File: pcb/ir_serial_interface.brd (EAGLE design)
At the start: 41.6 x 24.2 mm, 27 parts, among them IC1 PIC18LF2550, IC2 LP2992, Q2 MMBT6428LT1G, T1 PS401

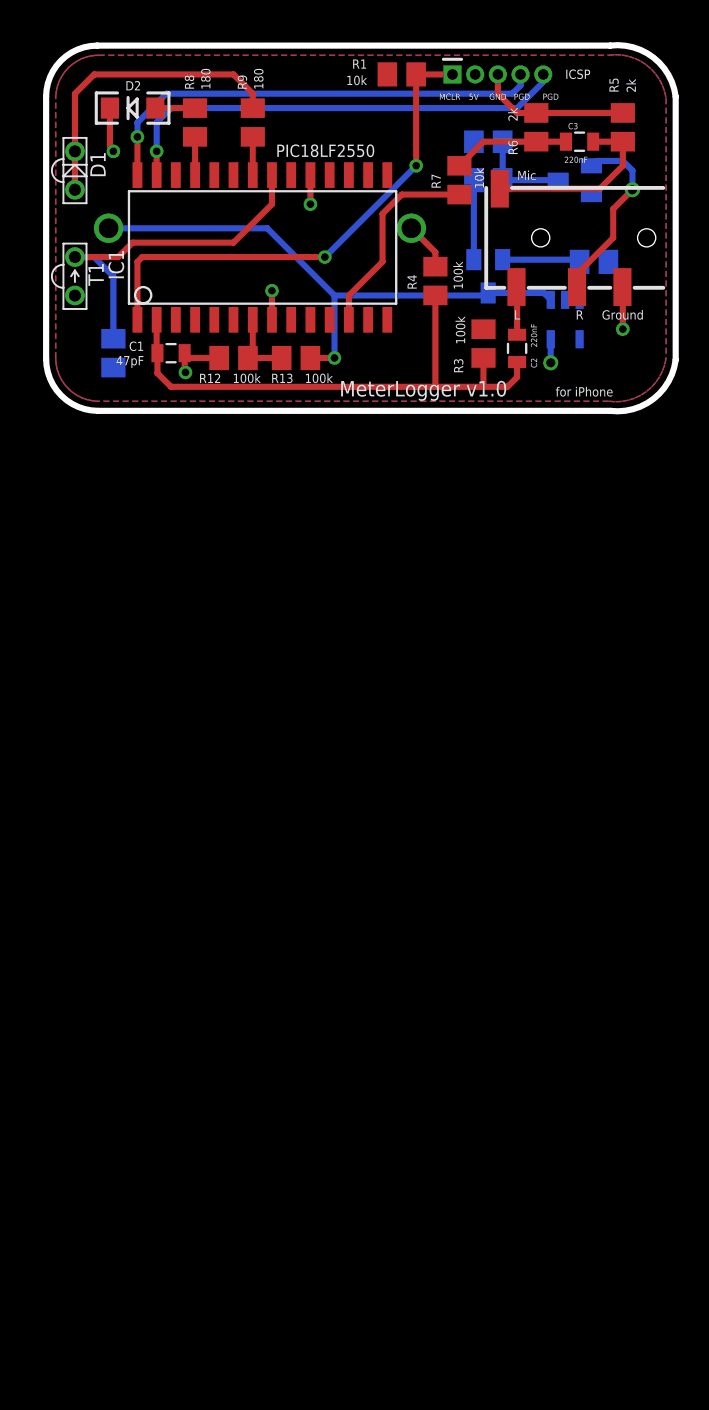
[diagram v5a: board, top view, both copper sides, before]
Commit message: PCB: Martens rettelser
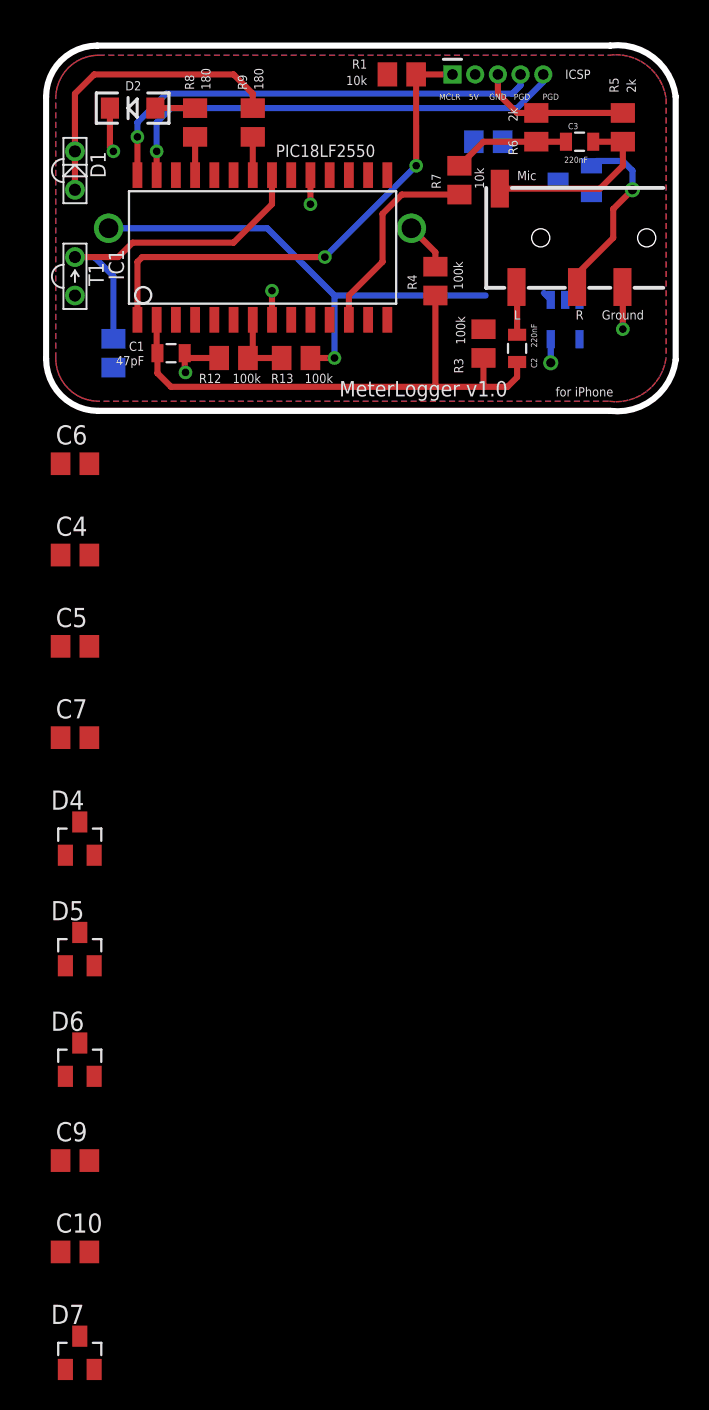
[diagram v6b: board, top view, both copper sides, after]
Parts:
- removed Q2: MMBT6428LT1G, transistor-npn:SOT23
- removed R10: 2k, resistor:M0805
- removed R11: 100k, resistor:M0805
- added C10, C7, C8, C9: 220nF, rcl:C0805
- added C5: 10uF, rcl:C0805
- added C6: 2200nF, rcl:C0805
- added D4, D5, D6: BAT65-05, diode:SOT23
- added D7: (no value), diode:SOT23
- C4: value 220nF -> 10nF
- moved C4 38.6 mm to (24.1, 16.5), flipped to the top
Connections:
- new net N$21: C10.2, D6.3, D7.3, IC2.3
- new net N$22: C4.1, IC2.4
- net +5V: now also C5.1
- net GND: now also C5.2, C6.2, C8.1, D3.1, D7.1; no longer R11.2
- net N$12: now also C7.1; no longer D3.1
- net N$13: now also C7.2, C9.1, D3.3, D4.1; no longer IC2.3, Q2.2, R11.1
- net N$17: now also C9.2, D5.3, D6.1; no longer Q2.1, R10.1
- net N$18: now also C10.1, C8.2, D4.3, D5.1; no longer C4.1, D3.3, R10.2
- net V+: now also C6.1; no longer Q2.3
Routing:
- net N$13: track 7.65 -> 0.00 mm
- net N$18: track 6.20 -> 0.00 mm
- net N$17: track 5.25 -> 0.00 mm
- net V+: track 37.0 -> 33.1 mm

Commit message: PCB: missing zener
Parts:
- D7: value (none) -> MMBZ5231BLT1G
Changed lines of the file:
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@@
 <element name="C9" library="rcl" package="C0805" value="220nF" x="24.13" y="-23.495"/>
 <element name="C10" library="rcl" package="C0805" value="220nF" x="24.13" y="-29.5275"/>
-<element name="D7" library="diode" package="SOT23" value="" x="24.4475" y="-36.195"/>
+<element name="D7" library="diode" package="SOT23" value="MMBZ5231BLT1G" x="24.4475" y="-36.195"/>
 </elements>
 <signals>

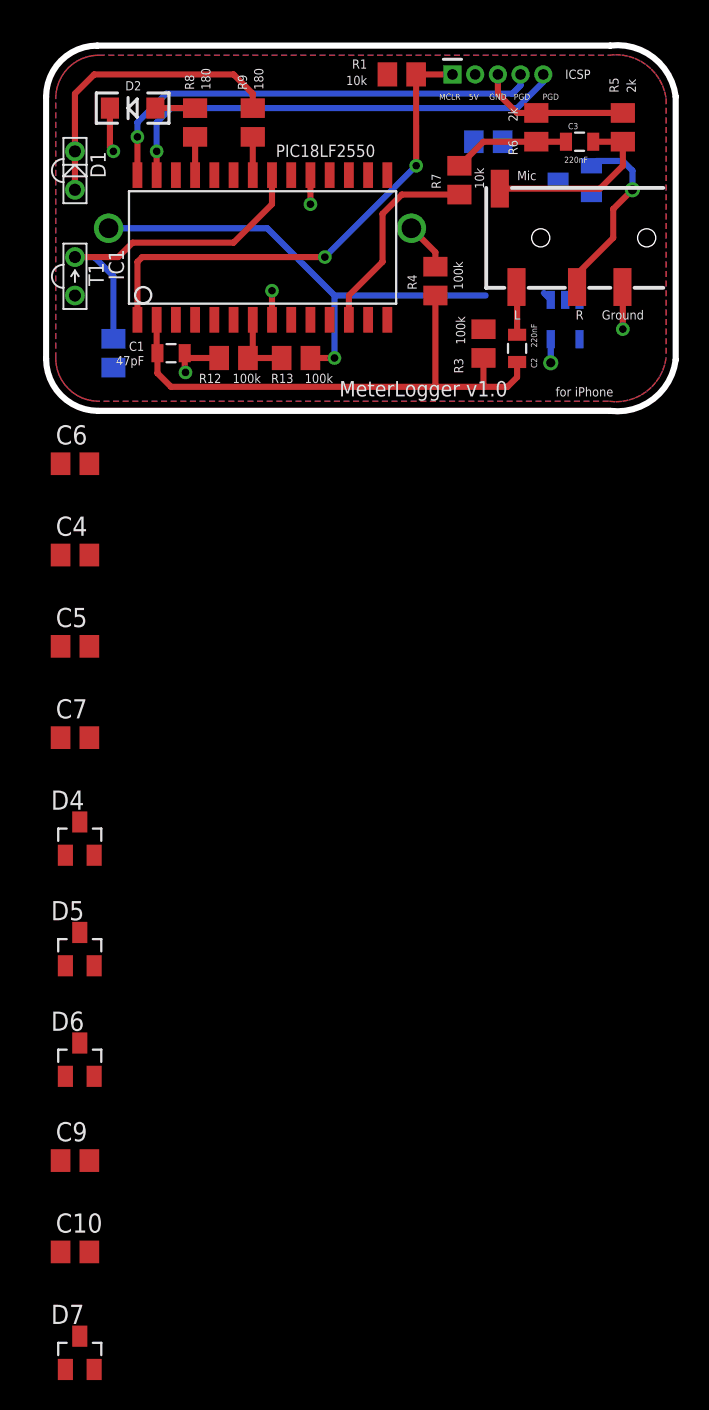
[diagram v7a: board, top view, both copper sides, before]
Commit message: PCB: Martens rettelser, layout done.
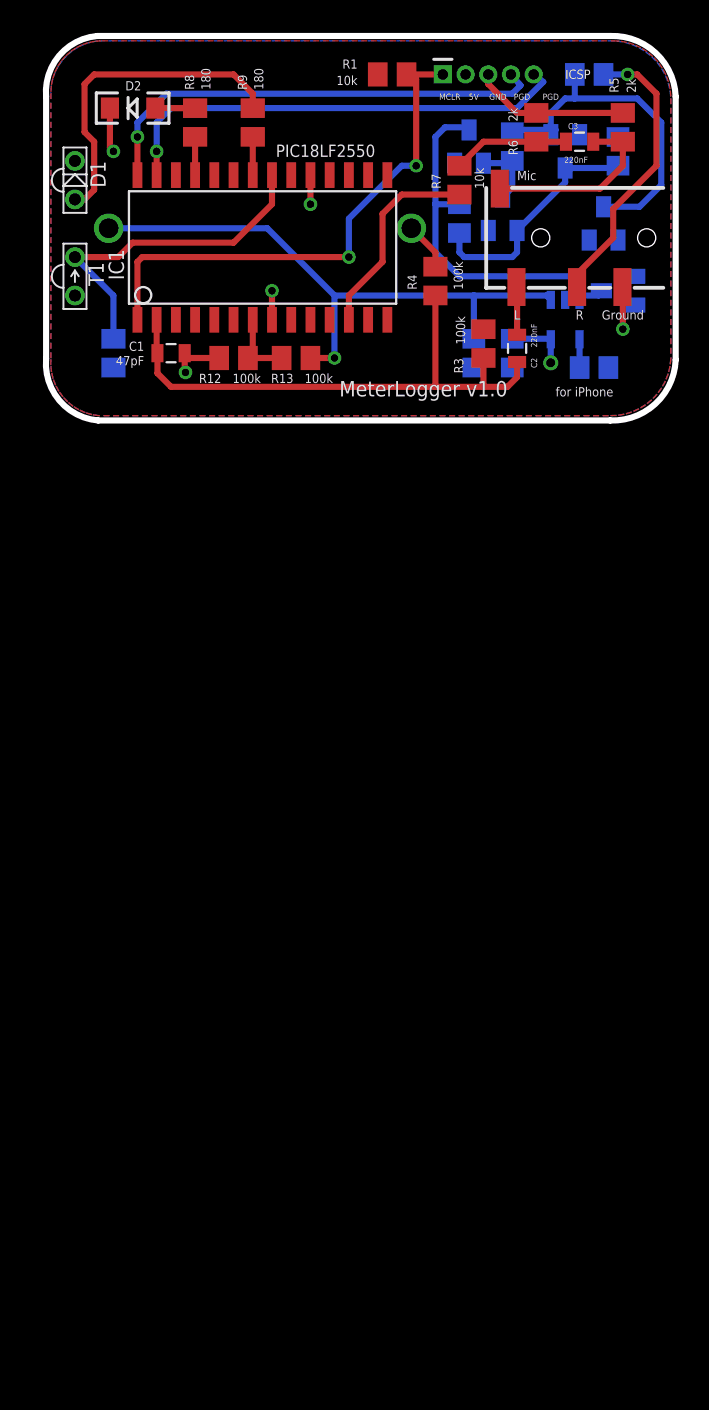
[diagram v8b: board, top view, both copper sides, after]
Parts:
- moved D7 78.7 mm to (60.0, 34.0), flipped to the bottom, turned to 270 degrees
- moved C9 73.0 mm to (53.0, 43.5), flipped to the bottom, turned to 270 degrees
- moved C10 72.8 mm to (49.5, 38.7), flipped to the bottom, turned to 90 degrees
- moved D6 65.6 mm to (50.2, 43.5), flipped to the bottom
- moved D5 56.0 mm to (52.4, 39.1), flipped to the bottom
- moved D4 55.6 mm to (56.5, 43.2), flipped to the bottom, turned to 180 degrees
- moved C7 55.4 mm to (58.1, 48.3), flipped to the bottom
- moved C4 36.5 mm to (58.4, 28.9), flipped to the bottom, turned to 180 degrees
- moved C5 34.8 mm to (53.0, 29.8), flipped to the bottom, turned to 270 degrees
- moved C6 27.3 mm to (50.5, 29.8), flipped to the bottom, turned to 270 degrees
- moved C8 8.60 mm to (60.0, 43.2), turned to 270 degrees
- moved D3 3.43 mm to (59.1, 38.4), turned to 0 degrees
- moved D1 0.63 mm to (24.1, 41.3)
- moved R1 0.63 mm to (45.1, 48.3)
- moved U$1 0.63 mm to (51.4, 48.3)
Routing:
- net N$21: track 0.00 -> 25.3 mm
- net N$13: track 0.00 -> 23.2 mm
- net N$18: track 0.00 -> 15.9 mm
- net N$12: track 11.9 -> 19.0 mm
- net V+: track 33.1 -> 39.7 mm
- net N$17: track 0.00 -> 5.56 mm
- net +5V: track 1.56 -> 4.11 mm
- net N$22: track 0.00 -> 1.88 mm
- net N$2: track 33.3 -> 34.9 mm
- net N$14: track 20.1 -> 21.6 mm
- net N$1: track 23.6 -> 22.8 mm
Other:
- board size 41.6 x 24.2 mm -> 41.6 x 25.4 mm
- board text added: "D3-D6: BAT65-05"
